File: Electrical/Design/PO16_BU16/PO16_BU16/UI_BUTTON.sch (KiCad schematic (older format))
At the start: 32 parts

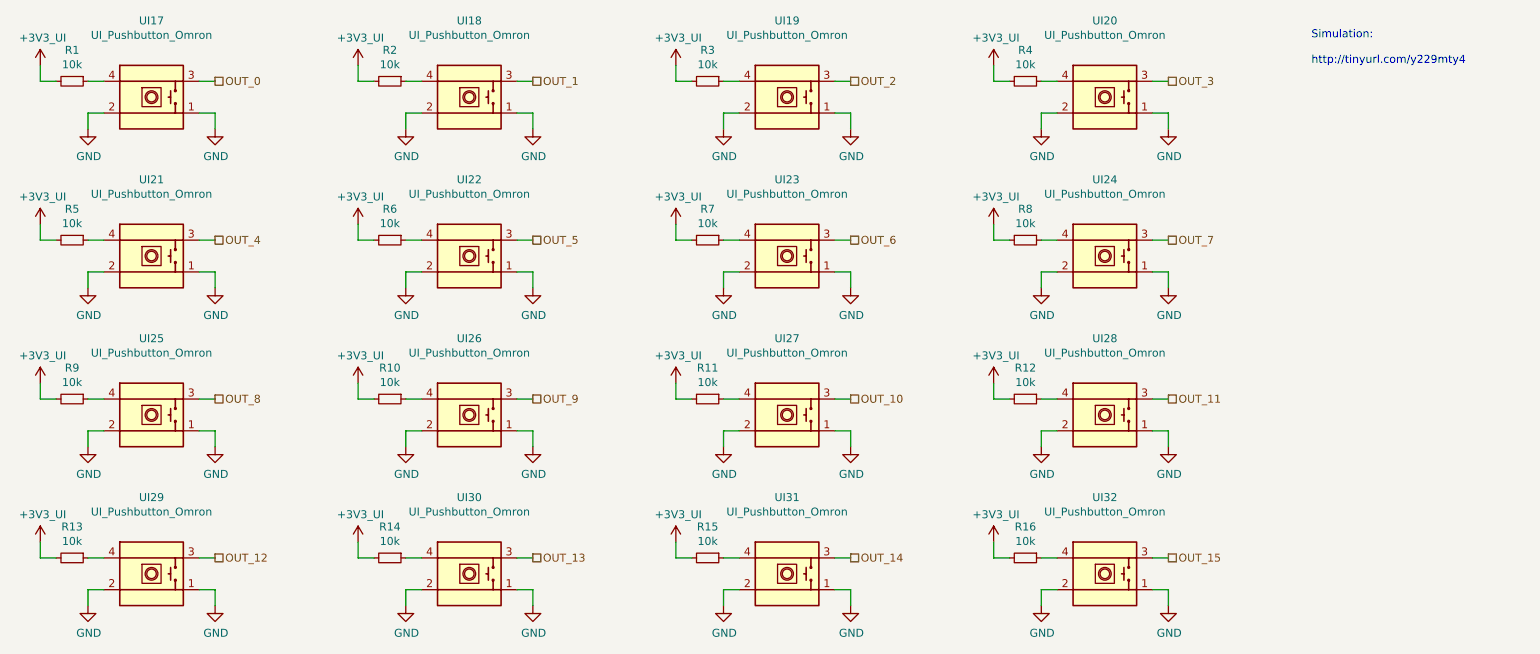
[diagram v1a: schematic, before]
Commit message: SUKU PO16_BU16 component values fixed, workflow updated
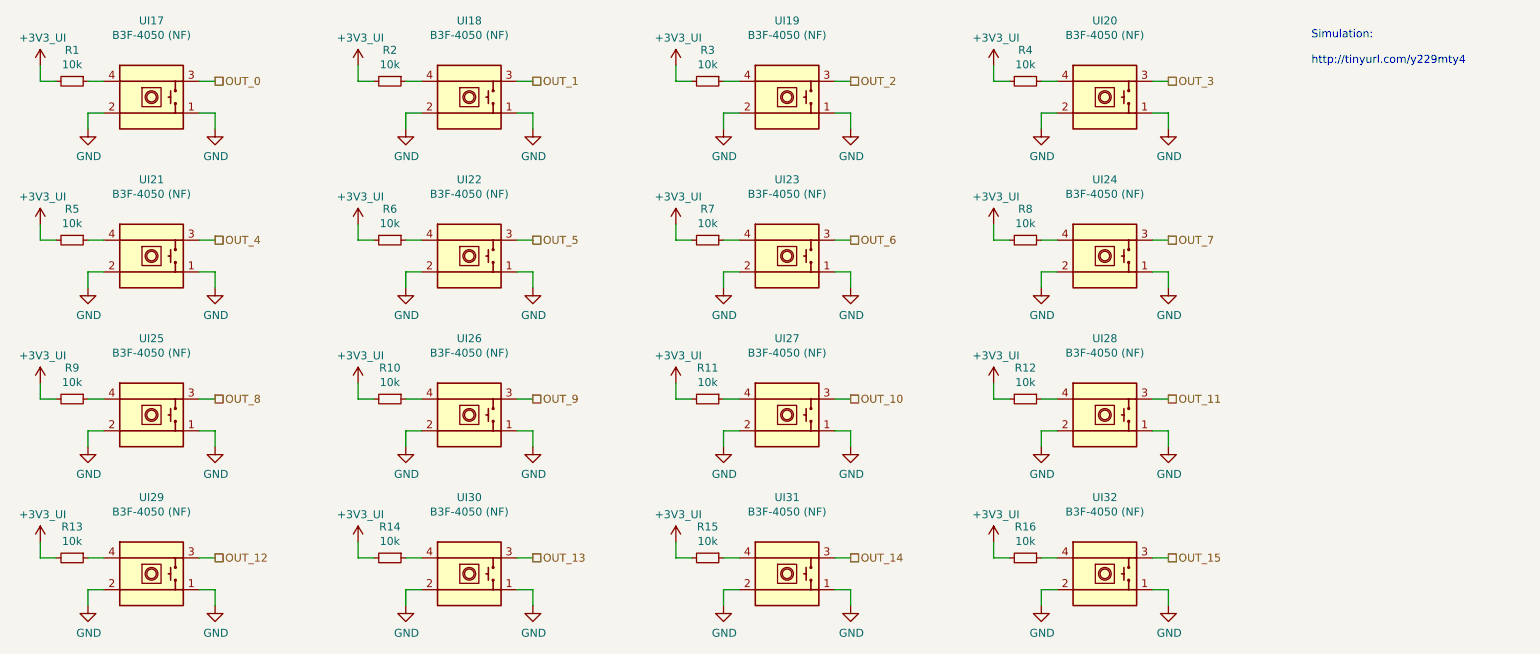
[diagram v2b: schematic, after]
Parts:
- UI17, UI18, UI19, UI20, UI21, UI22, UI23, UI24, UI25, UI26, UI27, UI28, UI29, UI30, UI31, UI32: value UI_Pushbutton_Omron -> B3F-4050 (NF)
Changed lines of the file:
@@
 P 2000 1500
 F 0 "UI17" H 2000 1981 50  0000 C CNN
-F 1 "UI_Pushbutton_Omron" H 2000 1890 50  0000 C CNN
+F 1 "B3F-4050 (NF)" H 2000 1890 50  0000 C CNN
 F 2 "suku_basics:UI_BUTTON_OMRON" H 1850 1660 50  0001 C CNN
 F 3 "~" H 2000 1960 50  0001 C CNN
@@
 P 4000 1500
 F 0 "UI18" H 4000 1981 50  0000 C CNN
-F 1 "UI_Pushbutton_Omron" H 4000 1890 50  0000 C CNN
+F 1 "B3F-4050 (NF)" H 4000 1890 50  0000 C CNN
 F 2 "suku_basics:UI_BUTTON_OMRON" H 3850 1660 50  0001 C CNN
 F 3 "~" H 4000 1960 50  0001 C CNN
@@
 P 6000 1500
 F 0 "UI19" H 6000 1981 50  0000 C CNN
-F 1 "UI_Pushbutton_Omron" H 6000 1890 50  0000 C CNN
+F 1 "B3F-4050 (NF)" H 6000 1890 50  0000 C CNN
 F 2 "suku_basics:UI_BUTTON_OMRON" H 5850 1660 50  0001 C CNN
 F 3 "~" H 6000 1960 50  0001 C CNN
@@
 P 8000 1500
 F 0 "UI20" H 8000 1981 50  0000 C CNN
-F 1 "UI_Pushbutton_Omron" H 8000 1890 50  0000 C CNN
+F 1 "B3F-4050 (NF)" H 8000 1890 50  0000 C CNN
 F 2 "suku_basics:UI_BUTTON_OMRON" H 7850 1660 50  0001 C CNN
 F 3 "~" H 8000 1960 50  0001 C CNN
@@
 P 2000 2500
 F 0 "UI21" H 2000 2981 50  0000 C CNN
-F 1 "UI_Pushbutton_Omron" H 2000 2890 50  0000 C CNN
+F 1 "B3F-4050 (NF)" H 2000 2890 50  0000 C CNN
 F 2 "suku_basics:UI_BUTTON_OMRON" H 1850 2660 50  0001 C CNN
 F 3 "~" H 2000 2960 50  0001 C CNN
@@
 P 4000 2500
 F 0 "UI22" H 4000 2981 50  0000 C CNN
-F 1 "UI_Pushbutton_Omron" H 4000 2890 50  0000 C CNN
+F 1 "B3F-4050 (NF)" H 4000 2890 50  0000 C CNN
 F 2 "suku_basics:UI_BUTTON_OMRON" H 3850 2660 50  0001 C CNN
 F 3 "~" H 4000 2960 50  0001 C CNN
@@
 P 6000 2500
 F 0 "UI23" H 6000 2981 50  0000 C CNN
-F 1 "UI_Pushbutton_Omron" H 6000 2890 50  0000 C CNN
+F 1 "B3F-4050 (NF)" H 6000 2890 50  0000 C CNN
 F 2 "suku_basics:UI_BUTTON_OMRON" H 5850 2660 50  0001 C CNN
 F 3 "~" H 6000 2960 50  0001 C CNN
@@
 P 8000 2500
 F 0 "UI24" H 8000 2981 50  0000 C CNN
-F 1 "UI_Pushbutton_Omron" H 8000 2890 50  0000 C CNN
+F 1 "B3F-4050 (NF)" H 8000 2890 50  0000 C CNN
 F 2 "suku_basics:UI_BUTTON_OMRON" H 7850 2660 50  0001 C CNN
 F 3 "~" H 8000 2960 50  0001 C CNN
@@
 P 2000 3500
 F 0 "UI25" H 2000 3981 50  0000 C CNN
-F 1 "UI_Pushbutton_Omron" H 2000 3890 50  0000 C CNN
+F 1 "B3F-4050 (NF)" H 2000 3890 50  0000 C CNN
 F 2 "suku_basics:UI_BUTTON_OMRON" H 1850 3660 50  0001 C CNN
 F 3 "~" H 2000 3960 50  0001 C CNN
@@
 P 4000 3500
 F 0 "UI26" H 4000 3981 50  0000 C CNN
-F 1 "UI_Pushbutton_Omron" H 4000 3890 50  0000 C CNN
+F 1 "B3F-4050 (NF)" H 4000 3890 50  0000 C CNN
 F 2 "suku_basics:UI_BUTTON_OMRON" H 3850 3660 50  0001 C CNN
 F 3 "~" H 4000 3960 50  0001 C CNN
@@
 P 6000 3500
 F 0 "UI27" H 6000 3981 50  0000 C CNN
-F 1 "UI_Pushbutton_Omron" H 6000 3890 50  0000 C CNN
+F 1 "B3F-4050 (NF)" H 6000 3890 50  0000 C CNN
 F 2 "suku_basics:UI_BUTTON_OMRON" H 5850 3660 50  0001 C CNN
 F 3 "~" H 6000 3960 50  0001 C CNN
@@
 P 8000 3500
 F 0 "UI28" H 8000 3981 50  0000 C CNN
-F 1 "UI_Pushbutton_Omron" H 8000 3890 50  0000 C CNN
+F 1 "B3F-4050 (NF)" H 8000 3890 50  0000 C CNN
 F 2 "suku_basics:UI_BUTTON_OMRON" H 7850 3660 50  0001 C CNN
 F 3 "~" H 8000 3960 50  0001 C CNN
@@
 P 2000 4500
 F 0 "UI29" H 2000 4981 50  0000 C CNN
-F 1 "UI_Pushbutton_Omron" H 2000 4890 50  0000 C CNN
+F 1 "B3F-4050 (NF)" H 2000 4890 50  0000 C CNN
 F 2 "suku_basics:UI_BUTTON_OMRON" H 1850 4660 50  0001 C CNN
 F 3 "~" H 2000 4960 50  0001 C CNN
@@
 P 4000 4500
 F 0 "UI30" H 4000 4981 50  0000 C CNN
-F 1 "UI_Pushbutton_Omron" H 4000 4890 50  0000 C CNN
+F 1 "B3F-4050 (NF)" H 4000 4890 50  0000 C CNN
 F 2 "suku_basics:UI_BUTTON_OMRON" H 3850 4660 50  0001 C CNN
 F 3 "~" H 4000 4960 50  0001 C CNN
@@
 P 6000 4500
 F 0 "UI31" H 6000 4981 50  0000 C CNN
-F 1 "UI_Pushbutton_Omron" H 6000 4890 50  0000 C CNN
+F 1 "B3F-4050 (NF)" H 6000 4890 50  0000 C CNN
 F 2 "suku_basics:UI_BUTTON_OMRON" H 5850 4660 50  0001 C CNN
 F 3 "~" H 6000 4960 50  0001 C CNN
@@
 P 8000 4500
 F 0 "UI32" H 8000 4981 50  0000 C CNN
-F 1 "UI_Pushbutton_Omron" H 8000 4890 50  0000 C CNN
+F 1 "B3F-4050 (NF)" H 8000 4890 50  0000 C CNN
 F 2 "suku_basics:UI_BUTTON_OMRON" H 7850 4660 50  0001 C CNN
 F 3 "~" H 8000 4960 50  0001 C CNN
